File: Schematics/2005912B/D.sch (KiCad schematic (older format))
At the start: 6 parts

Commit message: Finished up first draft of CAD for drawing 2005912B (i.e., AGC module A27-A29).  It passes ERC, but hasn't been meaningfully proofed.
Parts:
- gave numbers to parts that had none: 6
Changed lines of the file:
@@
 	19875 19275 19875 20475
 $Comp
-L AGC_DSKY:HierBody N?
+L AGC_DSKY:HierBody N4401
 U 1 1 5CC79017
 P 19975 19875
-AR Path="/5BA0299A/5CC79017" Ref="N?"  Part="1"
-AR Path="/5B9E2D11/5CC79017" Ref="N?"  Part="1"
-F 0 "N?" H 19960 19675 140 0001 C CNN
+AR Path="/5BA0299A/5CC79017" Ref="N4401"  Part="1"
+AR Path="/5B9E2D11/5CC79017" Ref="N601"  Part="1"
+AR Path="/5B9FC586/5CC79017" Ref="N3801"  Part="1"
+AR Path="/5B9FD210/5CC79017" Ref="N3901"  Part="1"
+AR Path="/5B9FED58/5CC79017" Ref="N4001"  Part="1"
+AR Path="/5B9FFB50/5CC79017" Ref="N4101"  Part="1"
+AR Path="/5BA009F6/5CC79017" Ref="N4201"  Part="1"
+AR Path="/5BA01950/5CC79017" Ref="N4301"  Part="1"
+AR Path="/5BA04D16/5CC79017" Ref="N4501"  Part="1"
+AR Path="/5BA05F52/5CC79017" Ref="N4601"  Part="1"
+AR Path="/5BA0726C/5CC79017" Ref="N4701"  Part="1"
+AR Path="/5BA0866A/5CC79017" Ref="N4801"  Part="1"
+AR Path="/5BA09B58/5CC79017" Ref="N4901"  Part="1"
+AR Path="/5BA0B184/5CC79017" Ref="N5001"  Part="1"
+AR Path="/5BA0C8F4/5CC79017" Ref="N5101"  Part="1"
+AR Path="/5BA0E1BA/5CC79017" Ref="N5201"  Part="1"
+AR Path="/5BA0FB88/5CC79017" Ref="N5301"  Part="1"
+AR Path="/5BA11664/5CC79017" Ref="N5401"  Part="1"
+F 0 "N5401" H 19960 19675 140 0001 C CNN
 F 1 "L" H 20150 19900 140 0000 C CNB
 F 2 "" H 19975 19875 140 0001 C CNN
@@
 $EndComp
 $Comp
-L AGC_DSKY:HierBody N?
+L AGC_DSKY:HierBody N4402
 U 1 1 5CC7901D
 P 19975 20325
-AR Path="/5BA0299A/5CC7901D" Ref="N?"  Part="1"
-AR Path="/5B9E2D11/5CC7901D" Ref="N?"  Part="1"
-F 0 "N?" H 19960 20125 140 0001 C CNN
+AR Path="/5BA0299A/5CC7901D" Ref="N4402"  Part="1"
+AR Path="/5B9E2D11/5CC7901D" Ref="N602"  Part="1"
+AR Path="/5B9FC586/5CC7901D" Ref="N3802"  Part="1"
+AR Path="/5B9FD210/5CC7901D" Ref="N3902"  Part="1"
+AR Path="/5B9FED58/5CC7901D" Ref="N4002"  Part="1"
+AR Path="/5B9FFB50/5CC7901D" Ref="N4102"  Part="1"
+AR Path="/5BA009F6/5CC7901D" Ref="N4202"  Part="1"
+AR Path="/5BA01950/5CC7901D" Ref="N4302"  Part="1"
+AR Path="/5BA04D16/5CC7901D" Ref="N4502"  Part="1"
+AR Path="/5BA05F52/5CC7901D" Ref="N4602"  Part="1"
+AR Path="/5BA0726C/5CC7901D" Ref="N4702"  Part="1"
+AR Path="/5BA0866A/5CC7901D" Ref="N4802"  Part="1"
+AR Path="/5BA09B58/5CC7901D" Ref="N4902"  Part="1"
+AR Path="/5BA0B184/5CC7901D" Ref="N5002"  Part="1"
+AR Path="/5BA0C8F4/5CC7901D" Ref="N5102"  Part="1"
+AR Path="/5BA0E1BA/5CC7901D" Ref="N5202"  Part="1"
+AR Path="/5BA0FB88/5CC7901D" Ref="N5302"  Part="1"
+AR Path="/5BA11664/5CC7901D" Ref="N5402"  Part="1"
+F 0 "N5402" H 19960 20125 140 0001 C CNN
 F 1 "G" H 20150 20325 140 0000 C CNB
 F 2 "" H 19975 20325 140 0001 C CNN
@@
 $EndComp
 $Comp
-L AGC_DSKY:HierBody N?
+L AGC_DSKY:HierBody N4403
 U 1 1 5CC79023
 P 21025 19850
-AR Path="/5BA0299A/5CC79023" Ref="N?"  Part="1"
-AR Path="/5B9E2D11/5CC79023" Ref="N?"  Part="1"
-F 0 "N?" H 21010 19650 140 0001 C CNN
+AR Path="/5BA0299A/5CC79023" Ref="N4403"  Part="1"
+AR Path="/5B9E2D11/5CC79023" Ref="N603"  Part="1"
+AR Path="/5B9FC586/5CC79023" Ref="N3803"  Part="1"
+AR Path="/5B9FD210/5CC79023" Ref="N3903"  Part="1"
+AR Path="/5B9FED58/5CC79023" Ref="N4003"  Part="1"
+AR Path="/5B9FFB50/5CC79023" Ref="N4103"  Part="1"
+AR Path="/5BA009F6/5CC79023" Ref="N4203"  Part="1"
+AR Path="/5BA01950/5CC79023" Ref="N4303"  Part="1"
+AR Path="/5BA04D16/5CC79023" Ref="N4503"  Part="1"
+AR Path="/5BA05F52/5CC79023" Ref="N4603"  Part="1"
+AR Path="/5BA0726C/5CC79023" Ref="N4703"  Part="1"
+AR Path="/5BA0866A/5CC79023" Ref="N4803"  Part="1"
+AR Path="/5BA09B58/5CC79023" Ref="N4903"  Part="1"
+AR Path="/5BA0B184/5CC79023" Ref="N5003"  Part="1"
+AR Path="/5BA0C8F4/5CC79023" Ref="N5103"  Part="1"
+AR Path="/5BA0E1BA/5CC79023" Ref="N5203"  Part="1"
+AR Path="/5BA0FB88/5CC79023" Ref="N5303"  Part="1"
+AR Path="/5BA11664/5CC79023" Ref="N5403"  Part="1"
+F 0 "N5403" H 21010 19650 140 0001 C CNN
 F 1 "M" H 20850 19850 140 0000 C CNB
 F 2 "" H 21025 19850 140 0001 C CNN
@@
 File: D.sch
 $Comp
-L AGC_DSKY:Resistor R?
+L AGC_DSKY:Resistor R4401
 U 1 1 5CC83163
 P 19900 16475
-AR Path="/5BA0299A/5CC83163" Ref="R?"  Part="1"
-AR Path="/5B9E2D11/5CC83163" Ref="R?"  Part="1"
-F 0 "R?" H 19875 16300 130 0001 C CNN
+AR Path="/5BA0299A/5CC83163" Ref="R4401"  Part="1"
+AR Path="/5B9E2D11/5CC83163" Ref="R601"  Part="1"
+AR Path="/5B9FC586/5CC83163" Ref="R3801"  Part="1"
+AR Path="/5B9FD210/5CC83163" Ref="R3901"  Part="1"
+AR Path="/5B9FED58/5CC83163" Ref="R4001"  Part="1"
+AR Path="/5B9FFB50/5CC83163" Ref="R4101"  Part="1"
+AR Path="/5BA009F6/5CC83163" Ref="R4201"  Part="1"
+AR Path="/5BA01950/5CC83163" Ref="R4301"  Part="1"
+AR Path="/5BA04D16/5CC83163" Ref="R4501"  Part="1"
+AR Path="/5BA05F52/5CC83163" Ref="R4601"  Part="1"
+AR Path="/5BA0726C/5CC83163" Ref="R4701"  Part="1"
+AR Path="/5BA0866A/5CC83163" Ref="R4801"  Part="1"
+AR Path="/5BA09B58/5CC83163" Ref="R4901"  Part="1"
+AR Path="/5BA0B184/5CC83163" Ref="R5001"  Part="1"
+AR Path="/5BA0C8F4/5CC83163" Ref="R5101"  Part="1"
+AR Path="/5BA0E1BA/5CC83163" Ref="R5201"  Part="1"
+AR Path="/5BA0FB88/5CC83163" Ref="R5301"  Part="1"
+AR Path="/5BA11664/5CC83163" Ref="R5401"  Part="1"
+F 0 "R5401" H 19875 16300 130 0001 C CNN
 F 1 "20K" H 19925 16700 130 0000 C CNN
 F 2 "" H 19900 16475 130 0001 C CNN
@@
 $EndComp
 $Comp
-L AGC_DSKY:Resistor R?
+L AGC_DSKY:Resistor R4402
 U 1 1 5CC83193
 P 22150 17275
-AR Path="/5BA0299A/5CC83193" Ref="R?"  Part="1"
-AR Path="/5B9E2D11/5CC83193" Ref="R?"  Part="1"
-F 0 "R?" H 22125 17100 130 0001 C CNN
+AR Path="/5BA0299A/5CC83193" Ref="R4402"  Part="1"
+AR Path="/5B9E2D11/5CC83193" Ref="R602"  Part="1"
+AR Path="/5B9FC586/5CC83193" Ref="R3802"  Part="1"
+AR Path="/5B9FD210/5CC83193" Ref="R3902"  Part="1"
+AR Path="/5B9FED58/5CC83193" Ref="R4002"  Part="1"
+AR Path="/5B9FFB50/5CC83193" Ref="R4102"  Part="1"
+AR Path="/5BA009F6/5CC83193" Ref="R4202"  Part="1"
+AR Path="/5BA01950/5CC83193" Ref="R4302"  Part="1"
+AR Path="/5BA04D16/5CC83193" Ref="R4502"  Part="1"
+AR Path="/5BA05F52/5CC83193" Ref="R4602"  Part="1"
+AR Path="/5BA0726C/5CC83193" Ref="R4702"  Part="1"
+AR Path="/5BA0866A/5CC83193" Ref="R4802"  Part="1"
+AR Path="/5BA09B58/5CC83193" Ref="R4902"  Part="1"
+AR Path="/5BA0B184/5CC83193" Ref="R5002"  Part="1"
+AR Path="/5BA0C8F4/5CC83193" Ref="R5102"  Part="1"
+AR Path="/5BA0E1BA/5CC83193" Ref="R5202"  Part="1"
+AR Path="/5BA0FB88/5CC83193" Ref="R5302"  Part="1"
+AR Path="/5BA11664/5CC83193" Ref="R5402"  Part="1"
+F 0 "R5402" H 22125 17100 130 0001 C CNN
 F 1 "2000" V 22250 17700 130 0000 C CNN
 F 2 "" H 22150 17275 130 0001 C CNN
@@
 $EndComp
 $Comp
-L AGC_DSKY:Capacitor-Polarized C?
+L AGC_DSKY:Capacitor-Polarized C4401
 U 1 1 5CC831E3
 P 20900 17225
-AR Path="/5BA0299A/5CC831E3" Ref="C?"  Part="1"
-AR Path="/5B9E2D11/5CC831E3" Ref="C?"  Part="1"
-F 0 "C?" H 21075 17425 130 0001 C CNN
+AR Path="/5BA0299A/5CC831E3" Ref="C4401"  Part="1"
+AR Path="/5B9E2D11/5CC831E3" Ref="C601"  Part="1"
+AR Path="/5B9FC586/5CC831E3" Ref="C3801"  Part="1"
+AR Path="/5B9FD210/5CC831E3" Ref="C3901"  Part="1"
+AR Path="/5B9FED58/5CC831E3" Ref="C4001"  Part="1"
+AR Path="/5B9FFB50/5CC831E3" Ref="C4101"  Part="1"
+AR Path="/5BA009F6/5CC831E3" Ref="C4201"  Part="1"
+AR Path="/5BA01950/5CC831E3" Ref="C4301"  Part="1"
+AR Path="/5BA04D16/5CC831E3" Ref="C4501"  Part="1"
+AR Path="/5BA05F52/5CC831E3" Ref="C4601"  Part="1"
+AR Path="/5BA0726C/5CC831E3" Ref="C4701"  Part="1"
+AR Path="/5BA0866A/5CC831E3" Ref="C4801"  Part="1"
+AR Path="/5BA09B58/5CC831E3" Ref="C4901"  Part="1"
+AR Path="/5BA0B184/5CC831E3" Ref="C5001"  Part="1"
+AR Path="/5BA0C8F4/5CC831E3" Ref="C5101"  Part="1"
+AR Path="/5BA0E1BA/5CC831E3" Ref="C5201"  Part="1"
+AR Path="/5BA0FB88/5CC831E3" Ref="C5301"  Part="1"
+AR Path="/5BA11664/5CC831E3" Ref="C5401"  Part="1"
+F 0 "C5401" H 21075 17425 130 0001 C CNN
 F 1 "6.8" H 21250 17050 130 0000 C CNN
 F 2 "" H 20900 17625 130 0001 C CNN

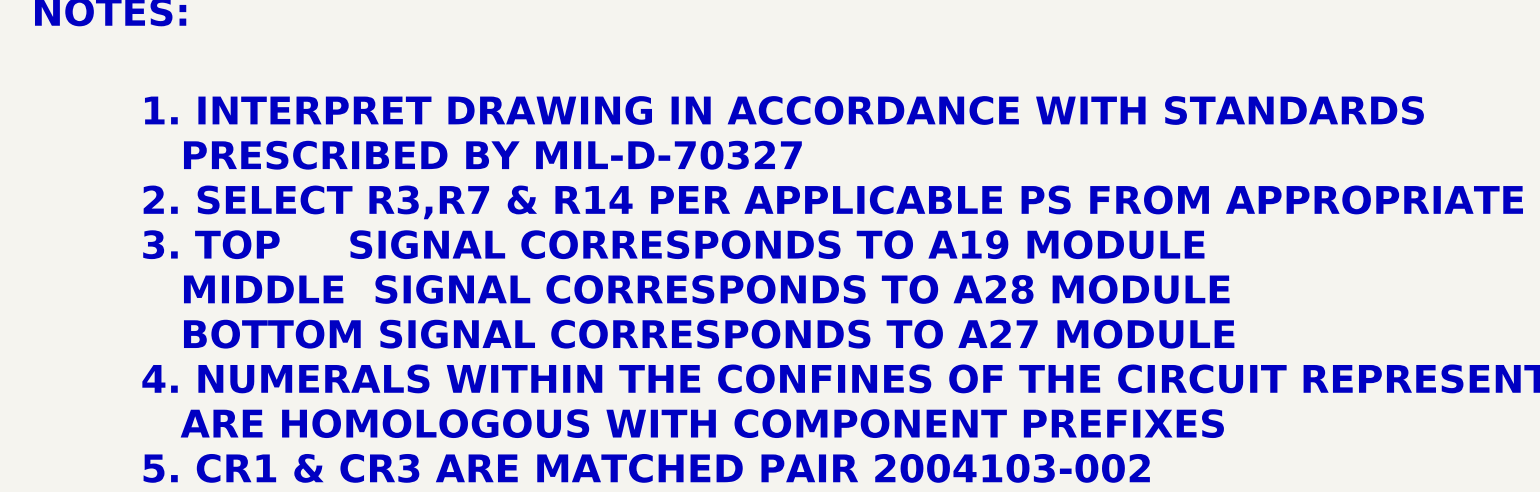
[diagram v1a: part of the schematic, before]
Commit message: Fixed a handful of bugs in the notes for 2005021C and 2005912B that just happened to catch my eye.
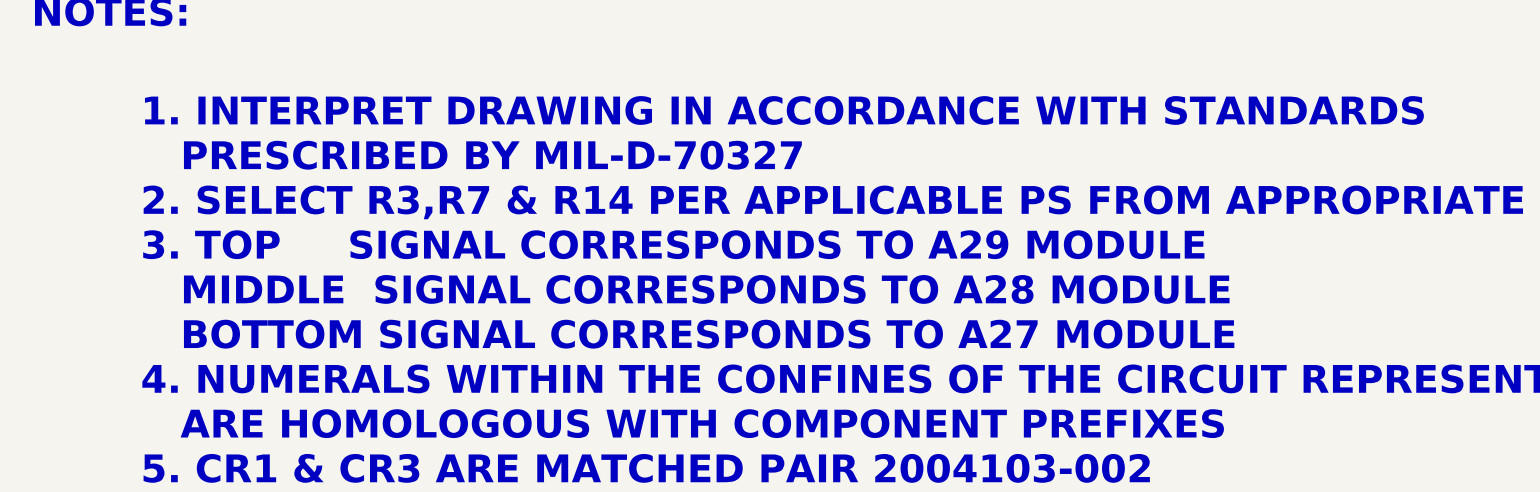
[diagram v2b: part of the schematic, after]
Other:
- note added: "1. INTERPRET DRAWING IN ACCORDANCE WITH STANDARDS\n PRESCRIBED BY MIL-D-70327\n2. SELECT R3,R7 & R14 PER APPLICABLE PS FROM APPROPRIATE CHART\n3. TOP SIGNAL CORRESPONDS TO A29 MODULE\n MIDDLE SIGNAL CORRESPONDS TO A28 MODULE\n BOTTOM SIGNAL CORRESPONDS TO A27 MODULE\n4. NUMERALS WITHIN THE CONFINES OF THE CIRCUIT REPRESENTATIONAL BLOCK\n ARE HOMOLOGOUS WITH COMPONENT PREFIXES\n5. CR1 & CR3 ARE MA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"
- note removed: "1. INTERPRET DRAWING IN ACCORDANCE WITH STANDARDS\n PRESCRIBED BY MIL-D-70327\n2. SELECT R3,R7 & R14 PER APPLICABLE PS FROM APPROPRIATE CHART\n3. TOP SIGNAL CORRESPONDS TO A19 MODULE\n MIDDLE SIGNAL CORRESPONDS TO A28 MODULE\n BOTTOM SIGNAL CORRESPONDS TO A27 MODULE\n4. NUMERALS WITHIN THE CONFINES OF THE CIRCUIT REPRESENTATIONAL BLOCK\n ARE HOMOLOGOUS WITH COMPONENT PREFIXES\n5. CR1 & CR3 ARE MA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"
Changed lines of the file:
@@
 $Descr E 44000 34000
 encoding utf-8
-Sheet 6 54
+Sheet 38 54
 Title ""
 Date ""
@@
 NOTES:
 Text Notes 1850 30350 0    140  ~ 28
-1. INTERPRET DRAWING IN ACCORDANCE WITH STANDARDS\n   PRESCRIBED BY MIL-D-70327\n2. SELECT R3,R7 & R14 PER APPLICABLE PS FROM APPROPRIATE CHART\n3. TOP     SIGNAL CORRESPONDS TO A19 MODULE\n   MIDDLE  SIGNAL CORRESPONDS TO A28 MODULE\n   BOTTOM SIGNAL CORRESPONDS TO A27 MODULE\n4. NUMERALS WITHIN THE CONFINES OF THE CIRCUIT REPRESENTATIONAL BLOCK\n   ARE HOMOLOGOUS WITH COMPONENT PREFIXES\n5. CR1 & CR3 ARE MATCHED PAIR 2004103-002
+1. INTERPRET DRAWING IN ACCORDANCE WITH STANDARDS\n   PRESCRIBED BY MIL-D-70327\n2. SELECT R3,R7 & R14 PER APPLICABLE PS FROM APPROPRIATE CHART\n3. TOP     SIGNAL CORRESPONDS TO A29 MODULE\n   MIDDLE  SIGNAL CORRESPONDS TO A28 MODULE\n   BOTTOM SIGNAL CORRESPONDS TO A27 MODULE\n4. NUMERALS WITHIN THE CONFINES OF THE CIRCUIT REPRESENTATIONAL BLOCK\n   ARE HOMOLOGOUS WITH COMPONENT PREFIXES\n5. CR1 & CR3 ARE MATCHED PAIR 2004103-002
 Text Notes 28075 22525 0    140  ~ 28
 R14
@@
 AR Path="/5BA0FB88/5CC79017" Ref="N5301"  Part="1"
 AR Path="/5BA11664/5CC79017" Ref="N5401"  Part="1"
-F 0 "N5401" H 19960 19675 140 0001 C CNN
+F 0 "N3801" H 19960 19675 140 0001 C CNN
 F 1 "L" H 20150 19900 140 0000 C CNB
 F 2 "" H 19975 19875 140 0001 C CNN
@@
 AR Path="/5BA0FB88/5CC7901D" Ref="N5302"  Part="1"
 AR Path="/5BA11664/5CC7901D" Ref="N5402"  Part="1"
-F 0 "N5402" H 19960 20125 140 0001 C CNN
+F 0 "N3802" H 19960 20125 140 0001 C CNN
 F 1 "G" H 20150 20325 140 0000 C CNB
 F 2 "" H 19975 20325 140 0001 C CNN
@@
 AR Path="/5BA0FB88/5CC79023" Ref="N5303"  Part="1"
 AR Path="/5BA11664/5CC79023" Ref="N5403"  Part="1"
-F 0 "N5403" H 21010 19650 140 0001 C CNN
+F 0 "N3803" H 21010 19650 140 0001 C CNN
 F 1 "M" H 20850 19850 140 0000 C CNB
 F 2 "" H 21025 19850 140 0001 C CNN
@@
 AR Path="/5BA0FB88/5CC83163" Ref="R5301"  Part="1"
 AR Path="/5BA11664/5CC83163" Ref="R5401"  Part="1"
-F 0 "R5401" H 19875 16300 130 0001 C CNN
+F 0 "R3801" H 19875 16300 130 0001 C CNN
 F 1 "20K" H 19925 16700 130 0000 C CNN
 F 2 "" H 19900 16475 130 0001 C CNN
@@
 AR Path="/5BA0FB88/5CC83193" Ref="R5302"  Part="1"
 AR Path="/5BA11664/5CC83193" Ref="R5402"  Part="1"
-F 0 "R5402" H 22125 17100 130 0001 C CNN
+F 0 "R3802" H 22125 17100 130 0001 C CNN
 F 1 "2000" V 22250 17700 130 0000 C CNN
 F 2 "" H 22150 17275 130 0001 C CNN
@@
 AR Path="/5BA0FB88/5CC831E3" Ref="C5301"  Part="1"
 AR Path="/5BA11664/5CC831E3" Ref="C5401"  Part="1"
-F 0 "C5401" H 21075 17425 130 0001 C CNN
+F 0 "C3801" H 21075 17425 130 0001 C CNN
 F 1 "6.8" H 21250 17050 130 0000 C CNN
 F 2 "" H 20900 17625 130 0001 C CNN
